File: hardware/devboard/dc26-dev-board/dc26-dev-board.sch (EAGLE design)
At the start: 92 parts, among them CN1 JST, IC1 STM32F411RET6, M10 STM32-Breakout-2, P1 SSSS811101, U1 ESP-WROOM-32, Y1 ABL-8.000MHZ-B2

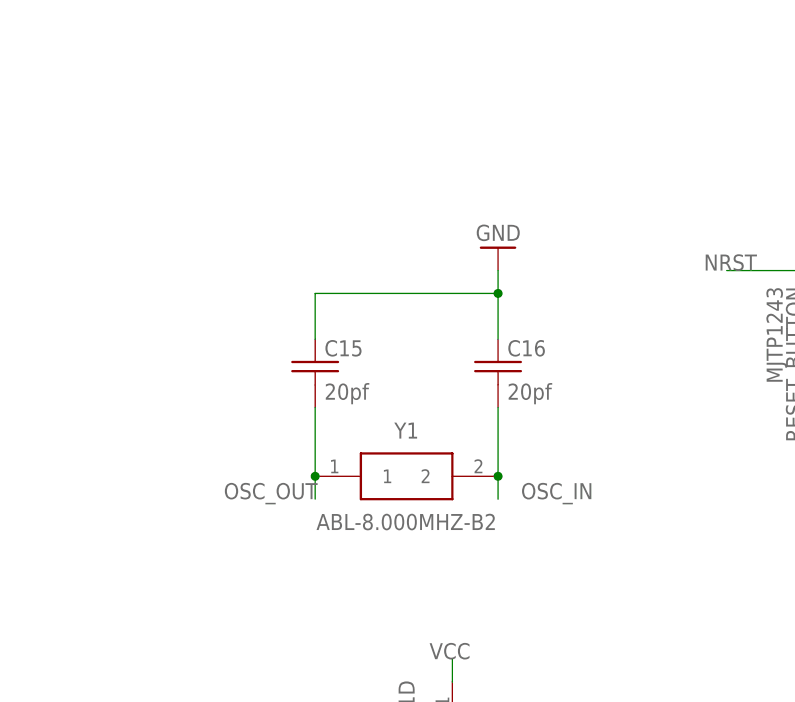
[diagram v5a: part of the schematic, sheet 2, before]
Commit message: added R9 to crystal moved logo and DN to tslik and bsilk layers
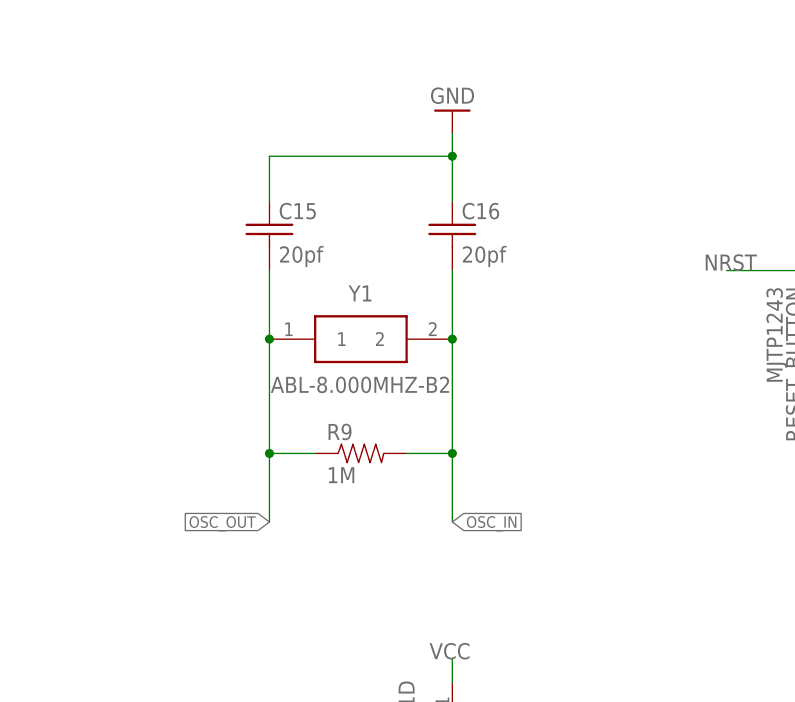
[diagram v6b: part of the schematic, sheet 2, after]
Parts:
- removed U$6: KRUX_LOGO, dc-26:KRUX_LOGO
- added R9: 1M, dc-26:RESISTOR0805-RES
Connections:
- net GND: now also P1.1
- net OSC_IN: now also R9.2
- net OSC_OUT: now also R9.1
- net VIN: now also P1.2; no longer P1.1
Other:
- moved on the sheet: C15, C16, Y1
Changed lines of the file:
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@@
 <part name="R8" library="dc-26" deviceset="RESISTOR" device="0805-RES" value="4K7"/>
 <part name="VDO" library="dc-26" deviceset="LD39100PU33RY" device=""/>
+<part name="R9" library="dc-26" deviceset="RESISTOR" device="0805-RES" value="1M"/>
+<part name="GND70" library="dc-26" deviceset="GND" device=""/>
 <part name="U$2" library="dc-26" deviceset="CMD_C0DE_LOGO" device=""/>
 <part name="U$3" library="dc-26" deviceset="DARKNET_D" device="D"/>
 <part name="U$4" library="dc-26" deviceset="DARKNET_N" device="N"/>
-<part name="U$6" library="dc-26" deviceset="KRUX_LOGO" device=""/>
 </parts>
 <sheets>
@@
 <instance part="GND9" gate="1" x="43.18" y="40.64" rot="R180"/>
 <instance part="VDO" gate="G$1" x="167.64" y="53.34" rot="R90"/>
+<instance part="GND70" gate="1" x="144.78" y="40.64"/>
 </instances>
 <busses>
@@
 <pinref part="GND7" gate="1" pin="GND"/>
 <wire x1="167.64" y1="91.44" x2="160.02" y2="91.44" width="0.1524" layer="91"/>
+</segment>
+<segment>
+<pinref part="P1" gate="G$1" pin="1"/>
+<wire x1="147.32" y1="48.26" x2="144.78" y2="48.26" width="0.1524" layer="91"/>
+<wire x1="144.78" y1="48.26" x2="144.78" y2="43.18" width="0.1524" layer="91"/>
+<pinref part="GND70" gate="1" pin="GND"/>
 </segment>
 </net>
@@
 <wire x1="152.4" y1="96.52" x2="144.78" y2="96.52" width="0.1524" layer="91"/>
 <junction x="152.4" y="96.52"/>
-<pinref part="P1" gate="G$1" pin="1"/>
 <wire x1="144.78" y1="96.52" x2="134.62" y2="96.52" width="0.1524" layer="91"/>
-<wire x1="147.32" y1="48.26" x2="144.78" y2="53.34" width="0.1524" layer="91"/>
 <wire x1="144.78" y1="53.34" x2="144.78" y2="96.52" width="0.1524" layer="91"/>
 <junction x="144.78" y="96.52"/>
@@
 <pinref part="VDO" gate="G$1" pin="VIN"/>
 <wire x1="170.18" y1="91.44" x2="170.18" y2="96.52" width="0.1524" layer="91"/>
+<pinref part="P1" gate="G$1" pin="2"/>
+<wire x1="147.32" y1="53.34" x2="144.78" y2="53.34" width="0.1524" layer="91"/>
 </segment>
 </net>
@@
 </plain>
 <instances>
-<instance part="Y1" gate="G$1" x="-20.32" y="101.6"/>
+<instance part="Y1" gate="G$1" x="-25.4" y="116.84"/>
 <instance part="IC1" gate="G$1" x="73.66" y="66.04"/>
 <instance part="C5" gate="G$1" x="-2.54" y="2.54"/>
@@
 <instance part="GND24" gate="1" x="17.78" y="45.72" rot="R90"/>
 <instance part="M10" gate="G$1" x="223.52" y="60.96"/>
-<instance part="C15" gate="G$1" x="-20.32" y="114.3"/>
-<instance part="C16" gate="G$1" x="0" y="114.3"/>
-<instance part="GND66" gate="1" x="0" y="127" rot="R180"/>
+<instance part="C15" gate="G$1" x="-25.4" y="129.54"/>
+<instance part="C16" gate="G$1" x="-5.08" y="129.54"/>
+<instance part="GND66" gate="1" x="-5.08" y="142.24" rot="R180"/>
 <instance part="C17" gate="G$1" x="114.3" y="-15.24"/>
 <instance part="GND65" gate="1" x="114.3" y="-22.86"/>
@@
 <instance part="GND69" gate="1" x="175.26" y="96.52"/>
 <instance part="R8" gate="G$1" x="43.18" y="134.62" rot="R270"/>
+<instance part="R9" gate="G$1" x="-15.24" y="104.14"/>
 </instances>
 <busses>
@@
 <segment>
 <pinref part="C15" gate="G$1" pin="1"/>
-<wire x1="-20.32" y1="116.84" x2="-20.32" y2="121.92" width="0.1524" layer="91"/>
-<wire x1="-20.32" y1="121.92" x2="0" y2="121.92" width="0.1524" layer="91"/>
+<wire x1="-25.4" y1="132.08" x2="-25.4" y2="137.16" width="0.1524" layer="91"/>
+<wire x1="-25.4" y1="137.16" x2="-5.08" y2="137.16" width="0.1524" layer="91"/>
 <pinref part="C16" gate="G$1" pin="1"/>
-<wire x1="0" y1="121.92" x2="0" y2="116.84" width="0.1524" layer="91"/>
-<wire x1="0" y1="121.92" x2="0" y2="124.46" width="0.1524" layer="91"/>
-<junction x="0" y="121.92"/>
+<wire x1="-5.08" y1="137.16" x2="-5.08" y2="132.08" width="0.1524" layer="91"/>
+<wire x1="-5.08" y1="137.16" x2="-5.08" y2="139.7" width="0.1524" layer="91"/>
+<junction x="-5.08" y="137.16"/>
 <pinref part="GND66" gate="1" pin="GND"/>
 </segment>
@@
 <segment>
 <pinref part="Y1" gate="G$1" pin="2"/>
-<wire x1="0" y1="101.6" x2="0" y2="99.06" width="0.1524" layer="91"/>
-<label x="2.54" y="99.06" size="1.778" layer="95"/>
+<wire x1="-5.08" y1="116.84" x2="-5.08" y2="104.14" width="0.1524" layer="91"/>
 <pinref part="C16" gate="G$1" pin="2"/>
-<wire x1="0" y1="101.6" x2="0" y2="109.22" width="0.1524" layer="91"/>
-<junction x="0" y="101.6"/>
+<wire x1="-5.08" y1="104.14" x2="-5.08" y2="96.52" width="0.1524" layer="91"/>
+<wire x1="-5.08" y1="116.84" x2="-5.08" y2="124.46" width="0.1524" layer="91"/>
+<junction x="-5.08" y="116.84"/>
+<pinref part="R9" gate="G$1" pin="2"/>
+<wire x1="-10.16" y1="104.14" x2="-5.08" y2="104.14" width="0.1524" layer="91"/>
+<junction x="-5.08" y="104.14"/>
+<label x="-5.08" y="96.52" size="1.27" layer="95" xref="yes"/>
 </segment>
 </net>
@@
 <segment>
 <pinref part="Y1" gate="G$1" pin="1"/>
-<wire x1="-20.32" y1="101.6" x2="-20.32" y2="99.06" width="0.1524" layer="91"/>
-<label x="-30.48" y="99.06" size="1.778" layer="95"/>
+<wire x1="-25.4" y1="116.84" x2="-25.4" y2="104.14" width="0.1524" layer="91"/>
 <pinref part="C15" gate="G$1" pin="2"/>
-<wire x1="-20.32" y1="101.6" x2="-20.32" y2="109.22" width="0.1524" layer="91"/>
-<junction x="-20.32" y="101.6"/>
+<wire x1="-25.4" y1="104.14" x2="-25.4" y2="96.52" width="0.1524" layer="91"/>
+<wire x1="-25.4" y1="116.84" x2="-25.4" y2="124.46" width="0.1524" layer="91"/>
+<junction x="-25.4" y="116.84"/>
+<pinref part="R9" gate="G$1" pin="1"/>
+<wire x1="-20.32" y1="104.14" x2="-25.4" y2="104.14" width="0.1524" layer="91"/>
+<junction x="-25.4" y="104.14"/>
+<label x="-25.4" y="96.52" size="1.27" layer="95" rot="R180" xref="yes"/>
 </segment>
 </net>
@@
 </plain>
 <instances>
-<instance part="U$2" gate="G$1" x="10.16" y="88.9"/>
-<instance part="U$3" gate="G$1" x="27.94" y="86.36"/>
-<instance part="U$4" gate="G$1" x="35.56" y="86.36"/>
-<instance part="U$6" gate="G$1" x="30.48" y="71.12"/>
+<instance part="U$2" gate="G$1" x="17.78" y="91.44"/>
+<instance part="U$3" gate="G$1" x="22.86" y="88.9"/>
+<instance part="U$4" gate="G$1" x="30.48" y="88.9"/>
 </instances>
 <busses>

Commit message: Board2 -  (#2)
* initial code compiling for esp32

* adding files

* more updates see last sheet for details

* added apa102

* started routing of devboard2

* power run not but not gpio

* after chatting with bunni

* fixed all board errors except air wires

* ran power to apa102

* fixed an overlap
moved logos onto board

* board sent to oshpark
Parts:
- removed Z1: CMDZ3L3_TR, dc-26:CMDZ3L3_TR
- added D1: (no value), dc-26:DIODESOD
- CN1: device dc-26:JST_2PIN-SMT-RA -> dc-26:JST_2PIN-THM-RA
- R1, R4: device dc-26:RESISTOR1206 -> dc-26:RESISTOR0805-RES
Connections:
- net ESP-RX: now also D1.C; no longer Z1.K
- net ESP-RX0: now also D1.A; no longer Z1.A
- net VCC: no longer ESP32PH.VCC
- net VCC0: no longer LINK1.VCC
- net VIN: now also ESP32PH.VCC, LINK1.VCC
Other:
- note added: "change log: 2/4/18: * Changed all resitors of package 1206 or 0805 * Moved STLink VCC to VIN just after fuse as ST Link only provides 3.3V and minor for charging circut is 3.45V * Changed JST package to JST-PH-2-THM-RA (same one we used in dc 25) * Moved ESP program header to sheet 1, VCC on esp programming header now goes to VIN after the charging circut * Change Zener diode on RX on esp to just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"
- note removed: "5V ST-Link In"
